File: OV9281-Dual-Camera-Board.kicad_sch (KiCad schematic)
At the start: 83 parts, among them J3 Conn_FFC_WE_68715014522_TWO-S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, Q1 BSS138PW, U1 ImageSensor_OV9281, U2 ImageSensor_OV9281, U3 NTS0104BQ, U4 NTB0104BQ, U5 TLV73318PDBVT, U6 TLV73312PDBVT, U7 TLV73328PDBVT, Y1 7C-24.000MBB-T, Y2 7C-24.000MBB-T

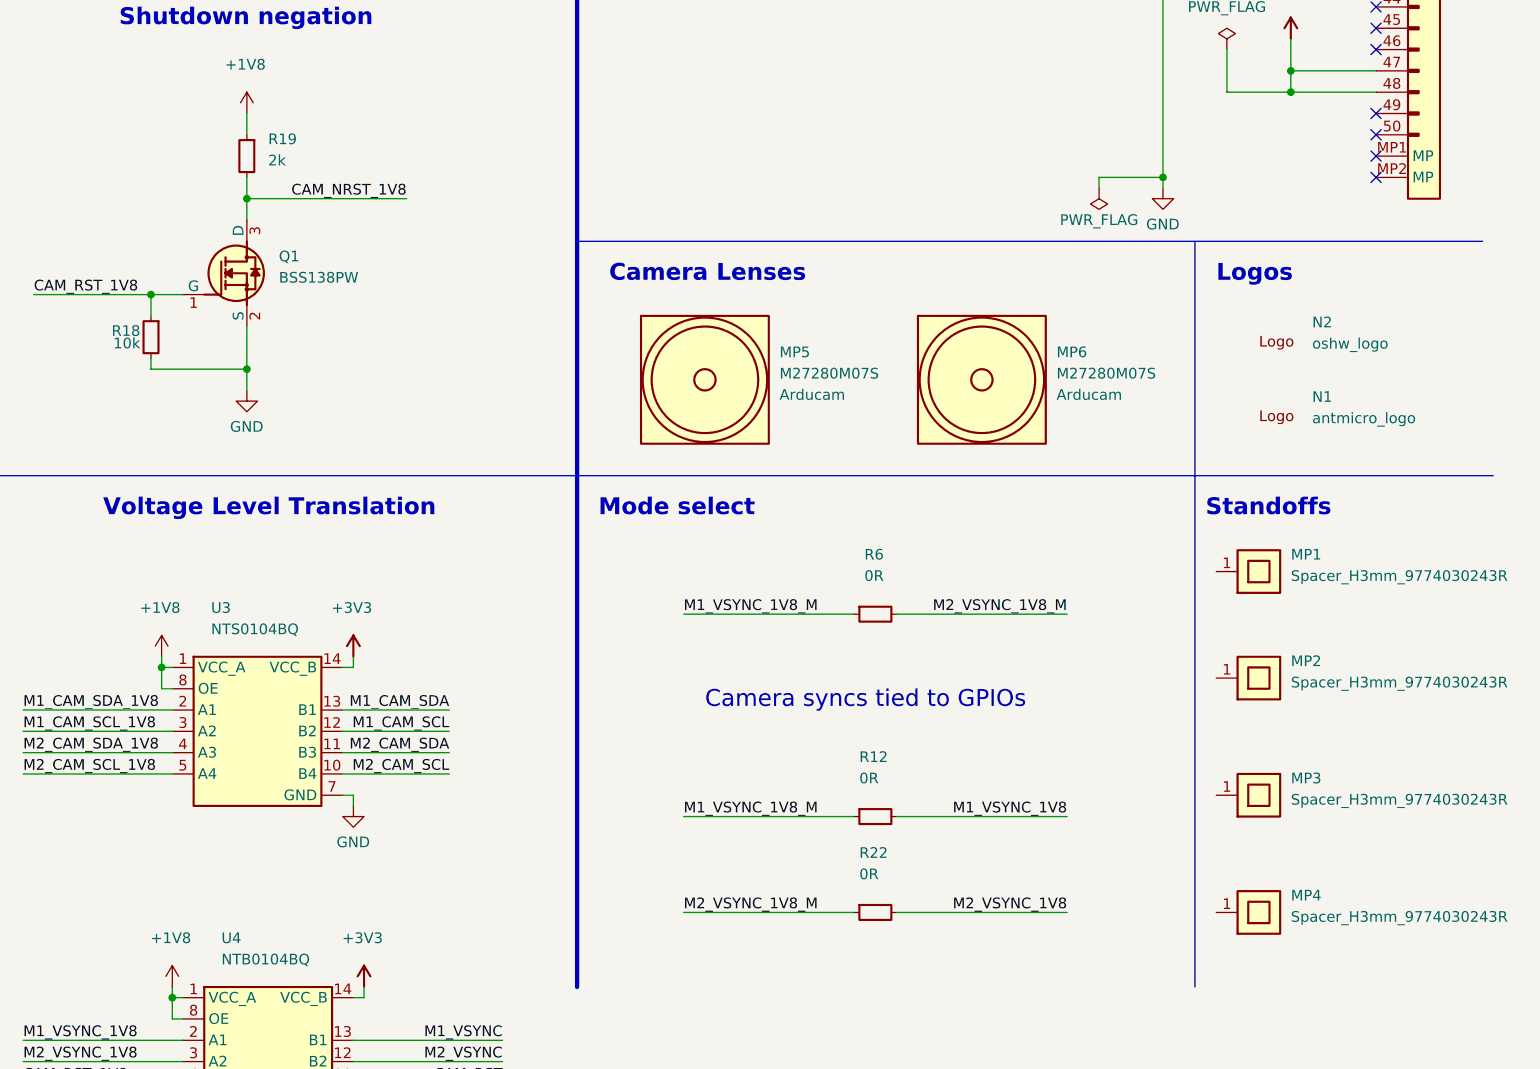
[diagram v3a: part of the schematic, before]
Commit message: [#49221] Replace BSS138PW with standardized BSS138AKA symbol
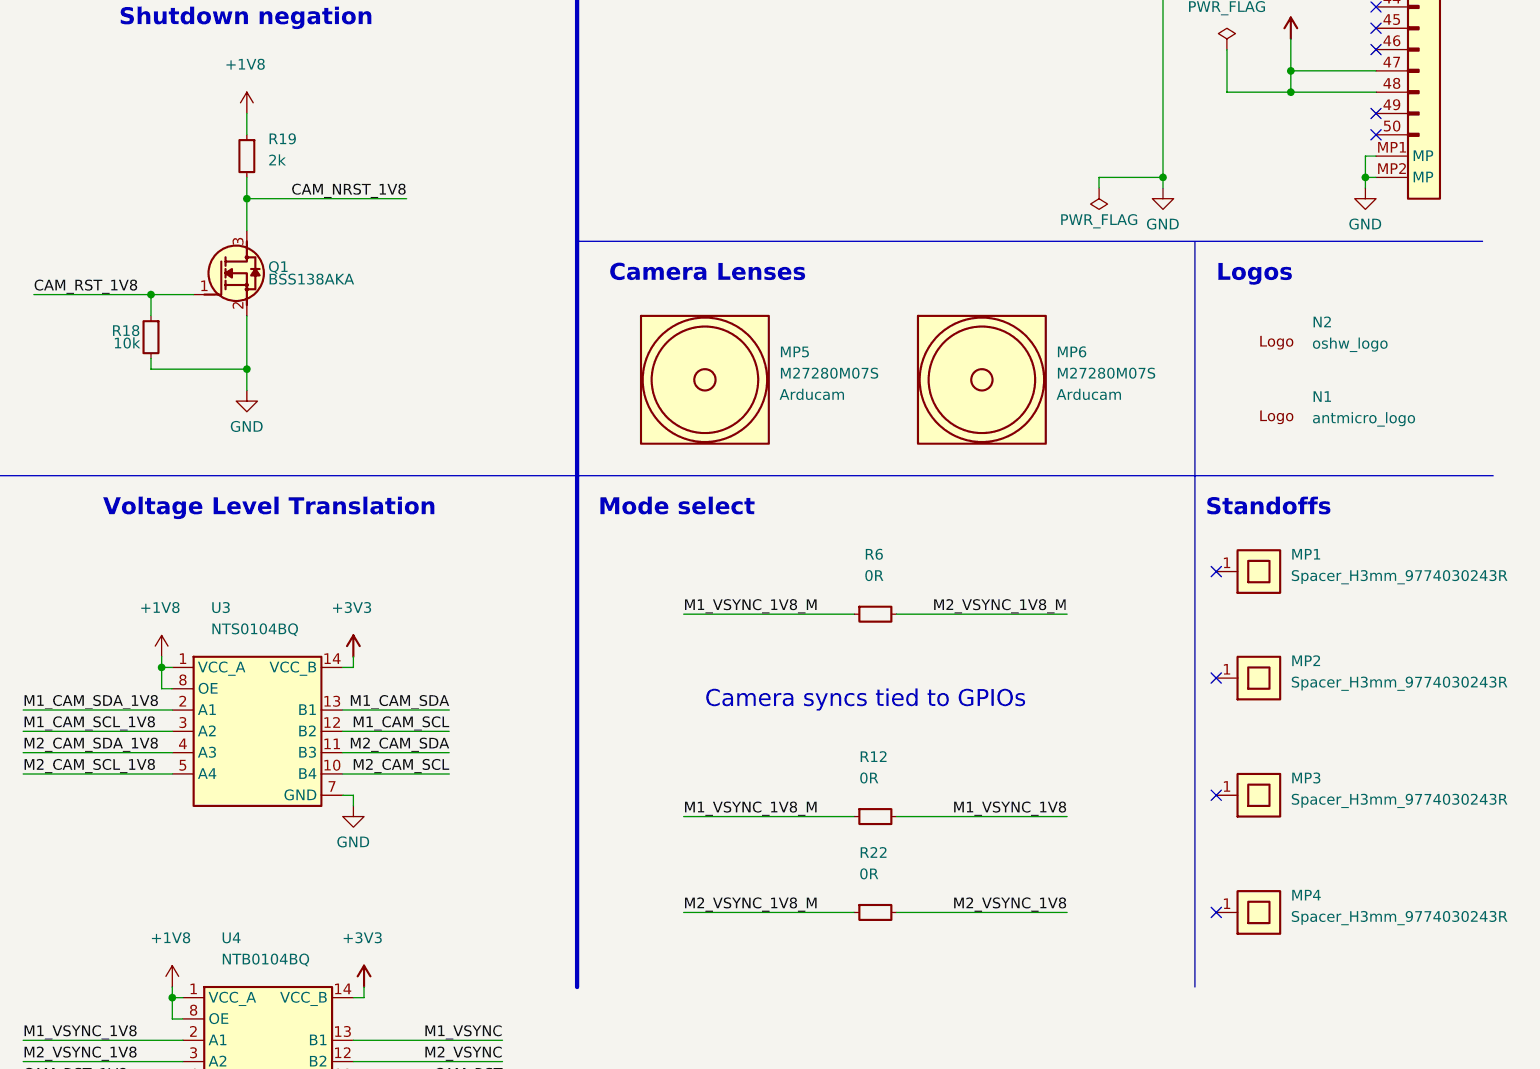
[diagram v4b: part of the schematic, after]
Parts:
- Q1: value BSS138PW -> BSS138AKA; footprint antmicro-footprints:SC70-3 -> antmicro-footprints:SOT-23-3; symbol antmicroTransistorsFETsMOSFETsSingle:BSS138PW -> antmicroTransistorsFETsMOSFETsSingle:BSS138AKA; MPN BSS138PW -> BSS138AKA; Manufacturer Nexperia -> ON Semiconductor
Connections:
- net GND: now also J3.MP1 (MP), J3.MP2 (MP)
- no-connect marks 49 -> 51
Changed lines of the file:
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@@
   (junction (at 201.93 116.84) (diameter 0) (color 0 0 0 0)
   )
+  (junction (at 393.7 156.21) (diameter 0) (color 0 0 0 0)
+  )
   (no_connect (at 199.39 113.03))
   (no_connect (at 394.97 59.69))
@@
   (no_connect (at 394.97 74.93))
   (no_connect (at 394.97 80.01))
+  (no_connect (at 375.92 229.87))
   (no_connect (at 199.39 97.79))
   (no_connect (at 199.39 92.71))
   (no_connect (at 394.97 102.87))
+  (no_connect (at 375.92 215.9))
   (no_connect (at 394.97 140.97))
+  (no_connect (at 375.92 243.84))
   (no_connect (at 199.39 100.33))
-  (no_connect (at 394.97 156.21))
   (no_connect (at 394.97 151.13))
   (no_connect (at 199.39 90.17))
@@
   (no_connect (at 394.97 148.59))
   (no_connect (at 394.97 133.35))
-  (no_connect (at 394.97 153.67))
   (no_connect (at 199.39 105.41))
   (no_connect (at 394.97 29.21))
@@
   (no_connect (at 394.97 31.75))
   (no_connect (at 394.97 34.29))
+  (no_connect (at 375.92 203.2))
   (no_connect (at 93.98 95.25))
   (no_connect (at 394.97 72.39))
@@
     (stroke (width 0) (type default) (color 0 0 0 0))
   )
-  (wire (pts (xy 260.35 173.99) (xy 260.35 179.07))
+  (wire (pts (xy 260.35 172.72) (xy 260.35 179.07))
     (stroke (width 0) (type default) (color 0 0 0 0))
   )
@@
     (stroke (width 0) (type default) (color 0 0 0 0))
   )
-  (wire (pts (xy 248.92 170.18) (xy 252.73 170.18))
+  (wire (pts (xy 248.92 170.18) (xy 254 170.18))
     (stroke (width 0) (type default) (color 0 0 0 0))
   )
@@
     (stroke (width 0) (type default) (color 0 0 0 0))
   )
+  (wire (pts (xy 393.7 153.67) (xy 394.97 153.67))
+    (stroke (width 0) (type default) (color 0 0 0 0))
+  )
   (wire (pts (xy 369.57 69.85) (xy 369.57 92.71))
     (stroke (width 0) (type default) (color 0 0 0 0))
@@
     (stroke (width 0) (type default) (color 0 0 0 0))
   )
+  (wire (pts (xy 393.7 156.21) (xy 393.7 157.48))
+    (stroke (width 0) (type default) (color 0 0 0 0))
+  )
   (wire (pts (xy 109.22 185.42) (xy 93.98 185.42))
     (stroke (width 0) (type default) (color 0 0 0 0))
@@
     (stroke (width 0) (type default) (color 0 0 0 0))
   )
+  (wire (pts (xy 393.7 156.21) (xy 394.97 156.21))
+    (stroke (width 0) (type default) (color 0 0 0 0))
+  )
   (wire (pts (xy 44.45 191.77) (xy 38.1 191.77))
     (stroke (width 0) (type default) (color 0 0 0 0))
@@
     (stroke (width 0) (type default) (color 0 0 0 0))
   )
-  (wire (pts (xy 260.35 161.29) (xy 260.35 158.75))
+  (wire (pts (xy 260.35 162.56) (xy 260.35 158.75))
     (stroke (width 0) (type default) (color 0 0 0 0))
   )
@@
     (stroke (width 0) (type default) (color 0 0 0 0))
   )
+  (wire (pts (xy 393.7 153.67) (xy 393.7 156.21))
+    (stroke (width 0) (type default) (color 0 0 0 0))
+  )
   (wire (pts (xy 137.16 161.29) (xy 137.16 166.37))
     (stroke (width 0) (type default) (color 0 0 0 0))
@@
     (pin "9")
   )
-  (symbol (lib_id "antmicroTransistorsFETsMOSFETsSingle:BSS138PW") (at 252.73 170.18 0) (unit 1)
-    (in_bom yes) (on_board yes) (fields_autoplaced)
-    (property "Reference" "Q1" (id 0) (at 264.16 166.3699 0)
-      (effects (font (size 1.27 1.27) (thickness 0.15)) (justify left bottom))
-    )
-    (property "Value" "BSS138PW" (id 1) (at 264.16 168.9099 0)
+  (symbol (lib_id "antmicroTransistorsFETsMOSFETsSingle:BSS138AKA") (at 254 170.18 0) (unit 1)
+    (in_bom yes) (on_board yes)
+    (property "Reference" "Q1" (id 0) (at 262.89 167.64 0)
       (effects (font (size 1.27 1.27) (thickness 0.15)) (justify left bottom))
     )
-    (property "Footprint" "antmicro-footprints:SC70-3" (id 2) (at 275.59 181.61 0)
+    (property "Value" "BSS138AKA" (id 1) (at 269.24 177.8 0)
       (effects (font (size 1.27 1.27) (thickness 0.15)) (justify left bottom) hide)
     )
-    (property "Datasheet" "https://assets.nexperia.com/documents/data-sheet/BSS138PW.pdf" (id 3) (at 275.59 184.15 0)
+    (property "Footprint" "antmicro-footprints:SOT-23-3" (id 2) (at 269.24 182.88 0)
       (effects (font (size 1.27 1.27) (thickness 0.15)) (justify left bottom) hide)
     )
-    (property "MPN" "BSS138PW" (id 4) (at 275.59 186.69 0)
+    (property "Datasheet" "https://www.onsemi.com/pub/Collateral/BSS138-D.PDF" (id 3) (at 269.24 185.42 0)
       (effects (font (size 1.27 1.27) (thickness 0.15)) (justify left bottom) hide)
     )
-    (property "Manufacturer" "Nexperia" (id 5) (at 275.59 189.23 0)
+    (property "MPN" "BSS138AKA" (id 4) (at 262.89 167.64 0)
+      (effects (font (size 1.27 1.27) (thickness 0.15)) (justify left top))
+    )
+    (property "Manufacturer" "ON Semiconductor" (id 5) (at 269.24 180.34 0)
       (effects (font (size 1.27 1.27) (thickness 0.15)) (justify left bottom) hide)
     )
-    (property "Author" "Antmicro" (id 6) (at 275.59 191.77 0)
+    (property "Author" "Antmicro" (id 6) (at 269.24 187.96 0)
       (effects (font (size 1.27 1.27) (thickness 0.15)) (justify left bottom) hide)
     )
-    (property "License" "Apache-2.0" (id 7) (at 275.59 194.31 0)
+    (property "License" "Apache-2.0" (id 7) (at 269.24 190.5 0)
       (effects (font (size 1.27 1.27) (thickness 0.15)) (justify left bottom) hide)
     )
@@
     (pin "1")
   )
+  (symbol (lib_id "antmicropower:GND") (at 393.7 157.48 0) (unit 1)
+    (in_bom yes) (on_board yes) (fields_autoplaced)
+    (property "Reference" "#PWR0121" (id 0) (at 393.7 163.83 0)
+      (effects (font (size 1.27 1.27) (thickness 0.15)) (justify left bottom) hide)
+    )
+    (property "Value" "GND" (id 1) (at 391.6898 162.56 0)
+      (effects (font (size 1.27 1.27) (thickness 0.15)) (justify left bottom))
+    )
+    (property "Footprint" "" (id 2) (at 402.59 165.1 0)
+      (effects (font (size 1.27 1.27) (thickness 0.15)) (justify left bottom) hide)
+    )
+    (property "Datasheet" "" (id 3) (at 402.59 170.18 0)
+      (effects (font (size 1.27 1.27) (thickness 0.15)) (justify left bottom) hide)
+    )
+    (property "Author" "Antmicro" (id 4) (at 402.59 165.1 0)
+      (effects (font (size 1.27 1.27) (thickness 0.15)) (justify left bottom) hide)
+    )
+    (property "License" "Apache-2.0" (id 5) (at 402.59 167.64 0)
+      (effects (font (size 1.27 1.27) (thickness 0.15)) (justify left bottom) hide)
+    )
+    (pin "1")
+  )
   (symbol (lib_id "antmicropower:PWR_FLAG") (at 107.95 189.23 90) (unit 1)
     (in_bom yes) (on_board yes) (fields_autoplaced)
@@
       (reference "#PWR0120") (unit 1) (value "GND") (footprint "")
     )
+    (path "/9b2af405-8e37-4d1d-9466-8e36b41525bc"
+      (reference "#PWR0121") (unit 1) (value "GND") (footprint "")
+    )
     (path "/00000000-0000-0000-0000-00005d5eeb0e"
       (reference "#PWR0122") (unit 1) (value "+2V8") (footprint "")
@@
     )
     (path "/00000000-0000-0000-0000-00005d7fe7cc"
-      (reference "Q1") (unit 1) (value "BSS138PW") (footprint "antmicro-footprints:SC70-3")
+      (reference "Q1") (unit 1) (value "BSS138AKA") (footprint "antmicro-footprints:SOT-23-3")
     )
     (path "/00000000-0000-0000-0000-00005d74ddde"

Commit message: [#49221] Replace QDHVQFN14 footprint with DHVQFN-14_1EP_2.5x3mm In NTS0104BQ and NTB0104BQ symbols
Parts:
- U3, U4: footprint antmicro-footprints:QDHVQFN14 -> antmicro-footprints:DHVQFN-14_1EP_2.5x3mm
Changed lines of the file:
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@@
       (effects (font (size 1.27 1.27) (thickness 0.15)) (justify left bottom) hide)
     )
-    (property "Footprint" "antmicro-footprints:QDHVQFN14" (id 2) (at 287.02 227.33 0)
+    (property "Footprint" "antmicro-footprints:DHVQFN-14_1EP_2.5x3mm" (id 2) (at 287.02 227.33 0)
       (effects (font (size 1.27 1.27) (thickness 0.15)) (justify left bottom) hide)
     )
@@
       (effects (font (size 1.27 1.27) (thickness 0.15)) (justify left bottom) hide)
     )
-    (property "Footprint" "antmicro-footprints:QDHVQFN14" (id 2) (at 288.29 269.24 0)
+    (property "Footprint" "antmicro-footprints:DHVQFN-14_1EP_2.5x3mm" (id 2) (at 288.29 269.24 0)
       (effects (font (size 1.27 1.27) (thickness 0.15)) (justify left bottom) hide)
     )
@@
     )
     (path "/00000000-0000-0000-0000-00005d7ca7df"
-      (reference "U3") (unit 1) (value "NTS0104BQ") (footprint "antmicro-footprints:QDHVQFN14")
+      (reference "U3") (unit 1) (value "NTS0104BQ") (footprint "antmicro-footprints:DHVQFN-14_1EP_2.5x3mm")
     )
     (path "/00000000-0000-0000-0000-00005da9696b"
-      (reference "U4") (unit 1) (value "NTB0104BQ") (footprint "antmicro-footprints:QDHVQFN14")
+      (reference "U4") (unit 1) (value "NTB0104BQ") (footprint "antmicro-footprints:DHVQFN-14_1EP_2.5x3mm")
     )
     (path "/00000000-0000-0000-0000-00005d715551"
